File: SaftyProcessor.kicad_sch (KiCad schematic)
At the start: 41 parts, among them J1 1935161, J2 1935161, J3 SJ2-35813B-SMT-TR, J4 SJ2-35813B-SMT-TR, SW1 SW_Push, U1 LM7805_TO220, U2 LM1117T-3.3, U3 ADS1118IDGS, U4 TXS0108EPW

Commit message: start adding switching pre-regulator
start isolating ground
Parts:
- removed C5: 10uf, Capacitor_SMD:C_0402_1005Metric, symbol Device:C
- removed C6: 0.1uf, Capacitor_SMD:C_0402_1005Metric, symbol Device:C
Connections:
- net GND_Safty renamed GND_Safty5V
- net GND_Safty5V: no longer C10.2, C9.2, U2.1 (GND)
- new net GND_Safty3.3V: C10.2, C9.2, U2.1 (GND)
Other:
- moved on the sheet: C1, C10, C2, C3, C4, C9, U1, U2

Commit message: sch progress
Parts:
- removed C11: 0.001uf, Capacitor_SMD:C_0402_1005Metric, symbol Device:C
- added C5: 0.1uf, Capacitor_SMD:C_0402_1005Metric, symbol Device:C
- added C6: 10uf 16v, Capacitor_SMD:C_0805_2012Metric, symbol Device:C
- added J5: 1935161, SamacSys_Parts:1935161, symbol SamacSys_Parts:1935161
- added R12, R17, R18: 680, Resistor_SMD:R_0402_1005Metric, symbol Device:R
- added R14, R15, R16: 1k, Resistor_SMD:R_0402_1005Metric, symbol Device:R
- added U4, U5, U6: TCMT1109, Package_SO:SOP-4_4.4x2.6mm_P1.27mm, symbol Isolator:TCMT1109
- C1: value 10uf -> 10uf 16v; footprint Capacitor_SMD:C_0402_1005Metric -> Capacitor_SMD:C_0805_2012Metric
- C10: value 10uf 16v -> 0.01uf
- C4: footprint Capacitor_SMD:C_0402_1005Metric -> Capacitor_SMD:C_0805_2012Metric
- C7, C8: value 10u -> 10uf 16v
- C9: value 0.1uf -> 0.01uf
- R5, R6: value 47k -> 47.5k
- renumbered R12 to R13, U4 to U7
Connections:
- net GND_Safty5V is gone; now on net GND_Safty: A1.29 (GND), A1.4 (GND), C1.2, C2.2, C3.2, C4.2, C7.2, C8.2, D1.2, D2.2, D3.2, D4.2, R11.1, R5.2, R6.2, SW1.1, U1.2 (GND), U3.3 (GND), U7.11 (GND)
- net 12V: no longer C1.1, C2.1, U1.1 (VI)
- net 3.3v_Safty: now also C8.1, C5.1; no longer C10.1, C9.1
- net 5v_Safty: now also R14.2, R15.2, R16.2
- net at R3.2, R5.1, U3.4 (AIN0): now also C6.1; no longer C7.1
- net at A1.28 (~{RESET}), R13.1, SW1.2: now also C9.1
- net at R4.2, R6.1, U3.6 (AIN2): now also C7.1; no longer C8.1
- net at A1.21 (A2): now also C10.1, J5.2, R16.1
- net at A1.22 (A3): now also R15.1, U6.4
- net at A1.23 (A4): now also R14.1, U4.4
- net at A1.24 (A5): now also R12.2
- net GND_Safty3.3V renamed GND_Safty
- net GND_Safty: now also C5.2, C6.2, J5.1, U4.3, U5.2, U6.3
- new net: R12.1, U5.1
- new net: R17.2, U4.1
- new net: R18.2, U6.1
- new net 8V: C1.1, C2.1, U1.1 (VI)
- new net DataFromSafty: U5.4
- new net DataGnd: U4.2, U5.3, U6.2
- new net DataToSafty: R17.1
- new net Fault: R18.1
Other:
- moved on the sheet: A1, D1, D2, D3, D4, D5, D6, D7, D8, J1, J2, J3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

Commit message: more sch updates
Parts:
- added D9: SMAJ24CA, Diode_SMD:D_SMA, symbol Diode:SMAJ24CA
- added NT1: NetTie_2, symbol Device:NetTie_2
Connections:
- net GND_Safty: now also D9.1 (A1), NT1.1
- net at A1.21 (A2), C10.1, J5.2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: now also D9.2 (A2)
- new net GND: NT1.2
- no-connect marks 0 -> 4
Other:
- sheet SSD ports: added RelayGND; removed GND
- note added: "Safty processor only supports 5v processors due to adc"
- moved on the sheet: C10, J5

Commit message: progress on pcb
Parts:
- added C50: 10uf 16v, Capacitor_SMD:C_0805_2012Metric, symbol Device:C
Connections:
- net 5v_Safty: now also C50.1
- net GND_Safty: now also C50.2
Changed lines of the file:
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@@
 	(wire
 		(pts
+			(xy 177.8 76.2) (xy 177.8 77.47)
+		)
+		(stroke
+			(width 0)
+			(type default)
+		)
+	)
+	(wire
+		(pts
 			(xy 118.11 181.61) (xy 118.11 187.96)
 		)
@@
 	(wire
 		(pts
+			(xy 177.8 68.58) (xy 177.8 67.31)
+		)
+		(stroke
+			(width 0)
+			(type default)
+		)
+	)
+	(wire
+		(pts
 			(xy 267.97 35.56) (xy 270.51 35.56)
 		)
@@
 	(symbol
 		(lib_id "power:GND3")
+		(at 177.8 77.47 0)
+		(unit 1)
+		(exclude_from_sim no)
+		(in_bom yes)
+		(on_board yes)
+		(dnp no)
+		(property "Reference" "#PWR080"
+			(at 177.8 83.82 0)
+			(effects
+				(font
+					(size 1.27 1.27)
+				)
+				(hide yes)
+			)
+		)
+		(property "Value" "GND_Safty"
+			(at 178.562 81.026 0)
+			(effects
+				(font
+					(size 1.27 1.27)
+				)
+				(justify left)
+			)
+		)
+		(property "Footprint" ""
+			(at 177.8 77.47 0)
+			(effects
+				(font
+					(size 1.27 1.27)
+				)
+				(hide yes)
+			)
+		)
+		(property "Datasheet" ""
+			(at 177.8 77.47 0)
+			(effects
+				(font
+					(size 1.27 1.27)
+				)
+				(hide yes)
+			)
+		)
+		(property "Description" "Power symbol creates a global label with name \"GND3\" , ground"
+			(at 177.8 77.47 0)
+			(effects
+				(font
+					(size 1.27 1.27)
+				)
+				(hide yes)
+			)
+		)
+		(pin "1"
+		)
+		(instances
+			(project "kiln"
+				(path "/e9c1836b-d16f-494a-819b-41549a786e18/9d216770-eb40-4527-939f-01f0f376c505"
+					(reference "#PWR080")
+					(unit 1)
+				)
+			)
+		)
+	)
+	(symbol
+		(lib_id "power:GND3")
 		(at 33.02 156.21 0)
 		(unit 1)
@@
 	(symbol
 		(lib_id "Device:C")
+		(at 177.8 72.39 0)
+		(unit 1)
+		(exclude_from_sim no)
+		(in_bom yes)
+		(on_board yes)
+		(dnp no)
+		(fields_autoplaced yes)
+		(property "Reference" "C50"
+			(at 181.61 71.1199 0)
+			(effects
+				(font
+					(size 1.27 1.27)
+				)
+				(justify left)
+			)
+		)
+		(property "Value" "10uf 16v"
+			(at 181.61 73.6599 0)
+			(effects
+				(font
+					(size 1.27 1.27)
+				)
+				(justify left)
+			)
+		)
+		(property "Footprint" "Capacitor_SMD:C_0805_2012Metric"
+			(at 178.7652 76.2 0)
+			(effects
+				(font
+					(size 1.27 1.27)
+				)
+				(hide yes)
+			)
+		)
+		(property "Datasheet" "https://www.mouser.com/ProductDetail/TAIYO-YUDEN/EMK212BJ106KG-T?qs=sGAEpiMZZMsh%252B1woXyUXjzXZPAgA2%252BEMKgT0bGGdQlI%3D"
+			(at 177.8 72.39 0)
+			(effects
+				(font
+					(size 1.27 1.27)
+				)
+				(hide yes)
+			)
+		)
+		(property "Description" "Unpolarized capacitor"
+			(at 177.8 72.39 0)
+			(effects
+				(font
+					(size 1.27 1.27)
+				)
+				(hide yes)
+			)
+		)
+		(pin "1"
+		)
+		(pin "2"
+		)
+		(instances
+			(project "kiln"
+				(path "/e9c1836b-d16f-494a-819b-41549a786e18/9d216770-eb40-4527-939f-01f0f376c505"
+					(reference "C50")
+					(unit 1)
+				)
+			)
+		)
+	)
+	(symbol
+		(lib_id "Device:C")
 		(at 130.81 177.8 0)
 		(unit 1)
@@
 					(unit 1)
 				)
+			)
+		)
+	)
+	(symbol
+		(lib_id "power:VPP")
+		(at 177.8 67.31 0)
+		(unit 1)
+		(exclude_from_sim no)
+		(in_bom yes)
+		(on_board yes)
+		(dnp no)
+		(fields_autoplaced yes)
+		(property "Reference" "#PWR079"
+			(at 177.8 71.12 0)
+			(effects
+				(font
+					(size 1.27 1.27)
+				)
+				(hide yes)
+			)
+		)
+		(property "Value" "5v_Safty"
+			(at 177.8 62.23 0)
+			(effects
+				(font
+					(size 1.27 1.27)
+				)
+			)
+		)
+		(property "Footprint" ""
+			(at 177.8 67.31 0)
+			(effects
+				(font
+					(size 1.27 1.27)
+				)
+				(hide yes)
+			)
+		)
+		(property "Datasheet" ""
+			(at 177.8 67.31 0)
+			(effects
+				(font
+					(size 1.27 1.27)
+				)
+				(hide yes)
+			)
+		)
+		(property "Description" "Power symbol creates a global label with name \"VPP\""
+			(at 177.8 67.31 0)
+			(effects
+				(font
+					(size 1.27 1.27)
+				)
+				(hide yes)
+			)
+		)
+		(pin "1"
+		)
+		(instances
+			(project "kiln"
+				(path "/e9c1836b-d16f-494a-819b-41549a786e18/9d216770-eb40-4527-939f-01f0f376c505"
+					(reference "#PWR079")
+					(unit 1)
+				)

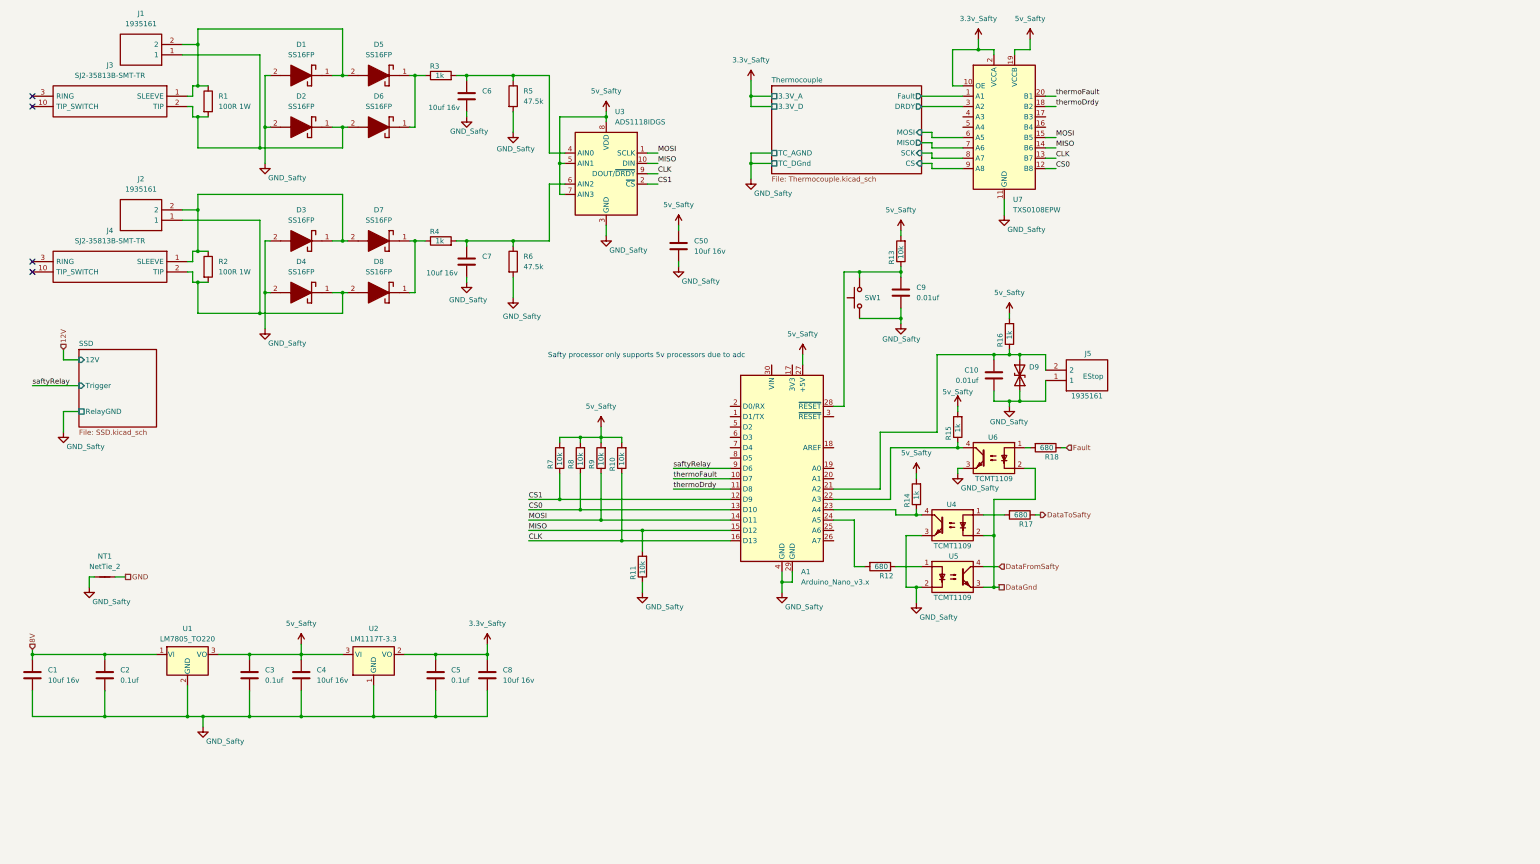
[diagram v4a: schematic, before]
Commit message: start switching to rp2040 and esp32
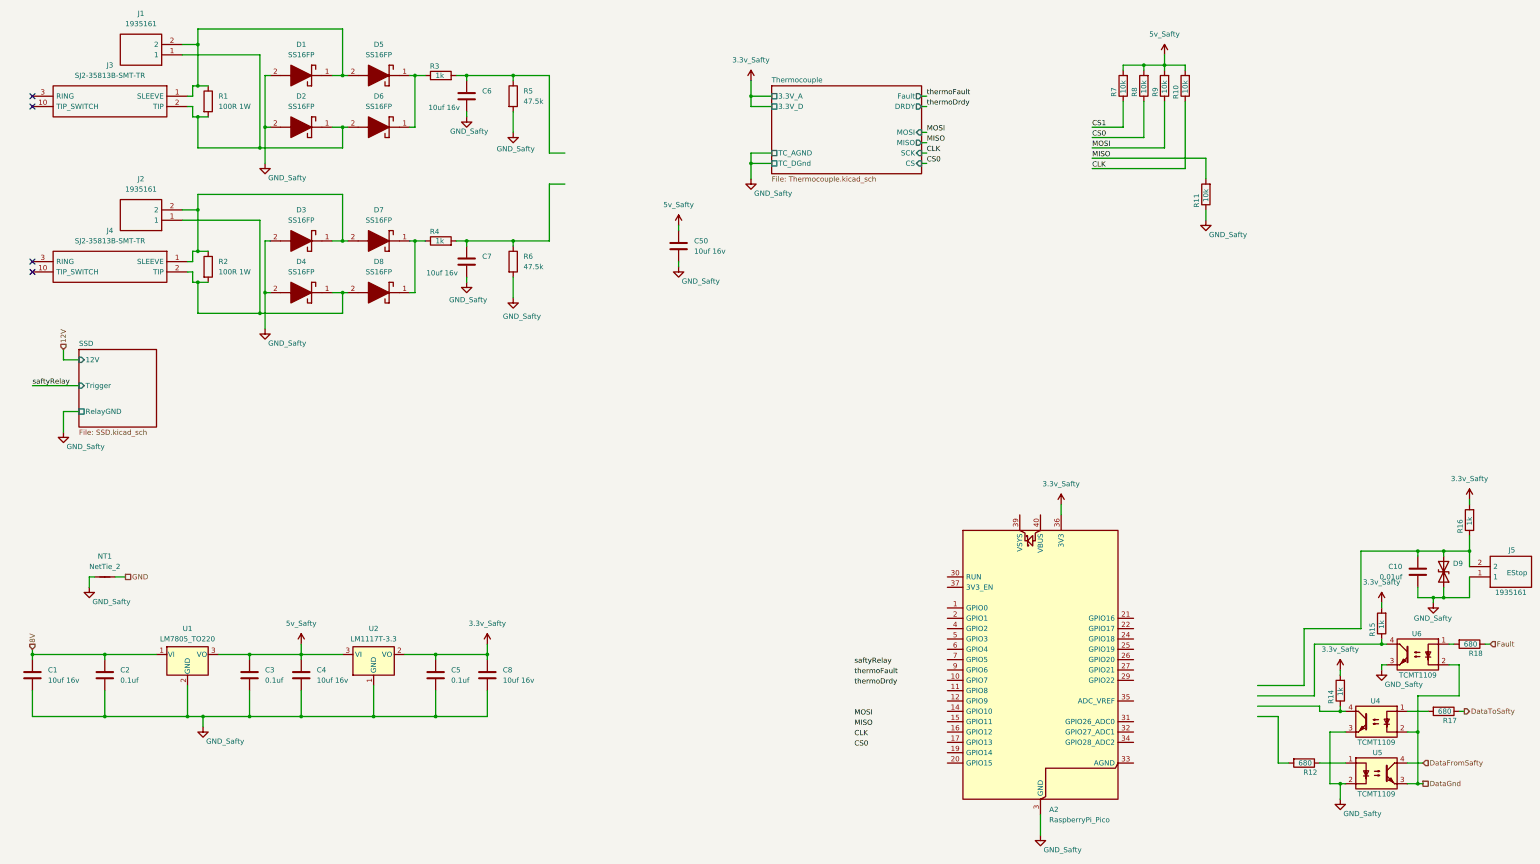
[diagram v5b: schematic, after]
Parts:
- removed A1: Arduino_Nano_v3.x, Module:Arduino_Nano, symbol MCU_Module:Arduino_Nano_v3.x
- removed C9: 0.01uf, Capacitor_SMD:C_0402_1005Metric, symbol Device:C
- removed R13: 10k, Resistor_SMD:R_0402_1005Metric, symbol Device:R
- removed SW1: SW_Push, Button_Switch_SMD:SW_Push_1P1T_NO_E-Switch_TL3301NxxxxxG, symbol Switch:SW_Push
- removed U3: ADS1118IDGS, Package_SO:VSSOP-10_3x3mm_P0.5mm, symbol Analog_ADC:ADS1118IDGS
- removed U7: TXS0108EPW, Package_SO:TSSOP-20_4.4x6.5mm_P0.65mm, symbol Logic_LevelTranslator:TXS0108EPW
- added A2: RaspberryPi_Pico, Module:RaspberryPi_Pico_Common_Unspecified, symbol MCU_Module:RaspberryPi_Pico
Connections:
- net 3.3v_Safty: now also R14.2, R15.2, R16.2, A2.36 (3V3)
- net 5v_Safty: no longer R14.2, R15.2, R16.2
- net GND_Safty: now also A2.13 (GND), A2.18 (GND), A2.23 (GND), A2.28 (GND), A2.3 (GND), A2.38 (GND), A2.8 (GND)
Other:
- note removed: "Safty processor only supports 5v processors due to adc"
- moved on the sheet: C10, D9, J5, R10, R11, R12, R14, R15, R16, R17, R18, R7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

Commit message: sch progress
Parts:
- removed C1, C4, C50, C6, C7, C8: 10uf 16v, Capacitor_SMD:C_0805_2012Metric, symbol Device:C
- removed C2, C3, C5: 0.1uf, Capacitor_SMD:C_0402_1005Metric, symbol Device:C
- removed D1, D2, D3, D4, D5, D6, D7, D8: SS16FP, SamacSys_Parts:SS12FP, symbol SamacSys_Parts:SS16FP
- removed D9: SMAJ24CA, Diode_SMD:D_SMA, symbol Diode:SMAJ24CA
- removed J1, J2: 1935161, SamacSys_Parts:1935161, symbol SamacSys_Parts:1935161
- removed J3, J4: SJ2-35813B-SMT-TR, SamacSys_Parts:SJ235813BSMTTR, symbol SamacSys_Parts:SJ2-35813B-SMT-TR
- removed NT1: NetTie_2, symbol Device:NetTie_2
- removed R1, R2: 100R 1W, Resistor_SMD:R_2512_6332Metric, symbol Device:R
- removed R10, R7, R8, R9: 10k, Resistor_SMD:R_0402_1005Metric, symbol Device:R
- removed R3, R4: 1k, Resistor_SMD:R_0402_1005Metric, symbol Device:R
- removed R5, R6: 47.5k, Resistor_SMD:R_0402_1005Metric, symbol Device:R
- removed U1: LM7805_TO220, Package_TO_SOT_THT:TO-220-3_Vertical, symbol Regulator_Linear:LM7805_TO220
- removed U2: LM1117T-3.3, Package_TO_SOT_THT:TO-220-3_Vertical, symbol Regulator_Linear:LM1117T-3.3
- added R31, R32, R33: 10k, Resistor_SMD:R_0402_1005Metric, symbol Device:R
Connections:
- net 3.3v_Safty: now also R31.2, R32.2, R33.2
- net CLK: now also A2.4 (GPIO2), R32.1
- net CS0: now also A2.2 (GPIO1), R31.1
- net GND_Safty: now also A2.33 (AGND)
- net MISO: now also A2.1 (GPIO0)
- net MOSI: now also A2.5 (GPIO3), R33.1
- net saftyRelay: now also A2.9 (GPIO6)
- net thermoDrdy: now also A2.11 (GPIO8)
- net thermoFault: now also A2.10 (GPIO7)
- net PicoTx: now reaches R12.2
- net PicoTx: now also A2.6 (GPIO4)
- net estop: now reaches C10.1, J5.2, R16.1
- net estop: now also A2.12 (GPIO9)
- net fault: now reaches R15.1, U6.4
- net fault: now also A2.14 (GPIO10)
- net PicoRx: now reaches R14.1, U4.4
- net PicoRx: now also A2.7 (GPIO5)
- net Current1: now reaches A2.31 (GPIO26_ADC0)
- net Current2: now reaches A2.32 (GPIO27_ADC1)
- net Current3: now reaches A2.34 (GPIO28_ADC2)
- net DataGnd renamed MainProcessorDataGnd
- no-connect marks 4 -> 0
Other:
- sheet SSD renamed SaftyRelay
- removed sheet Thermocouple
- added sheet CurrentSense (CurrentSense.kicad_sch)
- added sheet CurrentSense1 (CurrentSense.kicad_sch)
- added sheet CurrentSense2 (CurrentSense.kicad_sch)
- added sheet SaftyThermocouple (Thermocouple.kicad_sch)
- moved on the sheet: A2, C10, J5, R12, R14, R15, R16, R17, R18, U4, U5, U6

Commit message: progress. still need to finish review
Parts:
- added R89, R90: 10k, Resistor_SMD:R_0402_1005Metric, symbol Device:R
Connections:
- net 3.3v_Safty: now also R89.2, R90.2
- net thermoDrdy: now also R90.1
- net thermoFault: now also R89.1
